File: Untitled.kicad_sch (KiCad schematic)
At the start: 20 parts, among them J1 Battery Connector, J2 Top Screw Terminal, J3 Bottom Screw Terminal, Q1 Q_NMOS_DGS, Q2 Q_NMOS_DGS, Q3 Q_NMOS_DGS, U1 XIAO-ESP32-S3-SMD, U3 LSM6DSO32, U4 MS5611-01BA

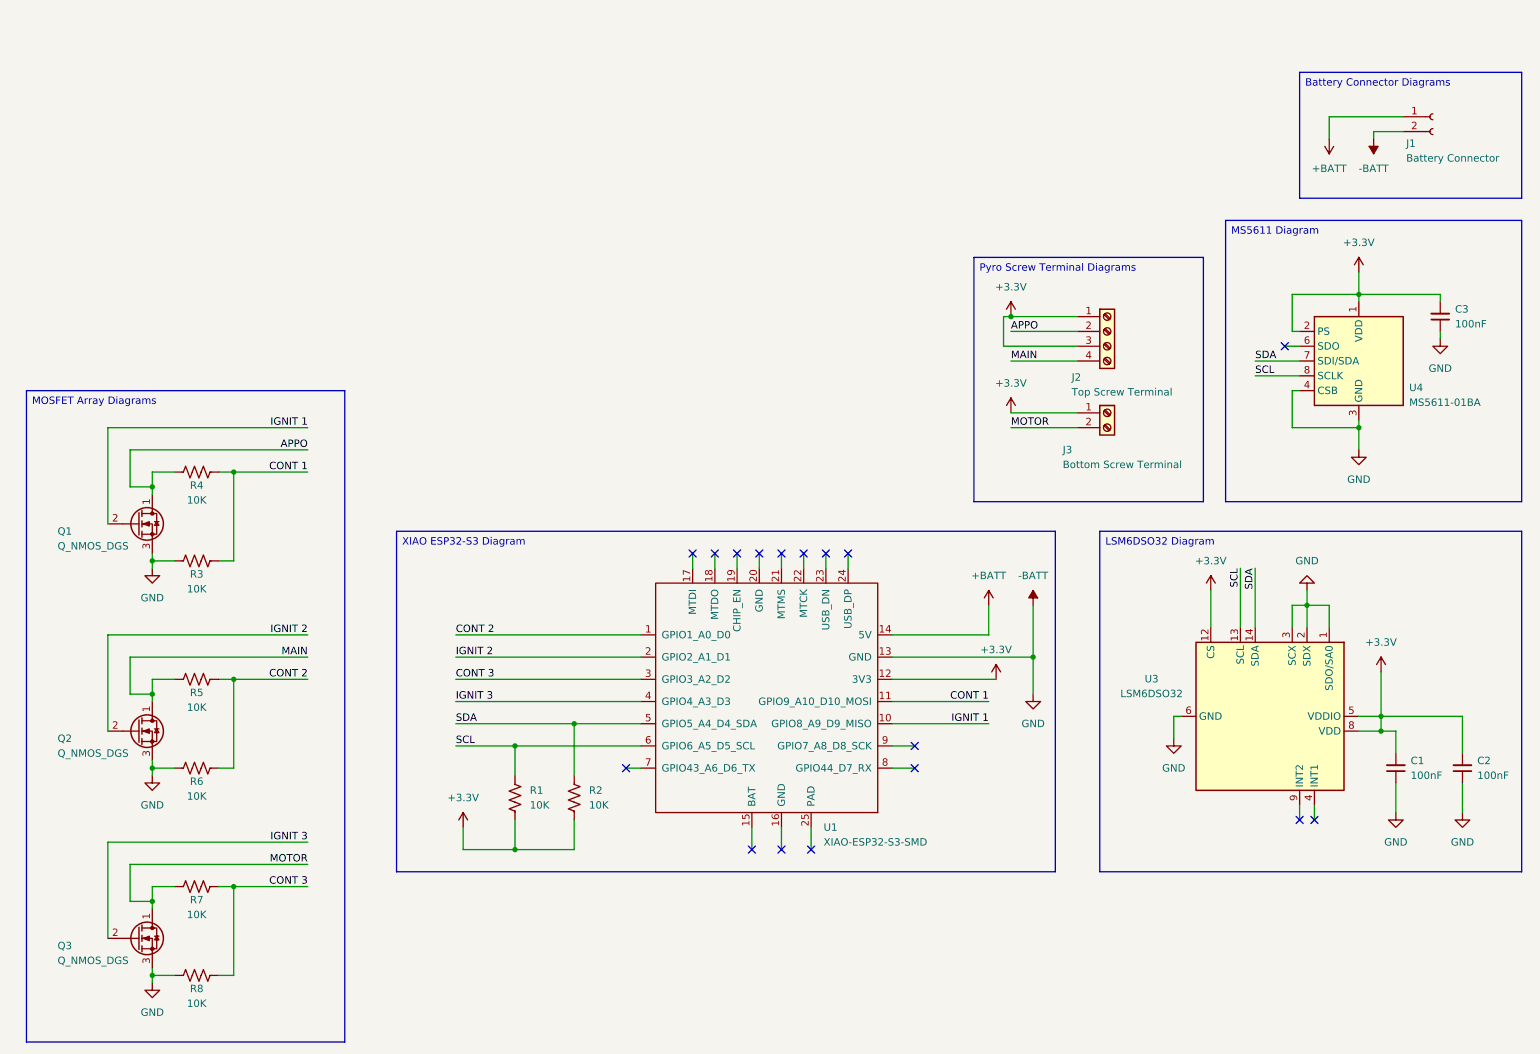
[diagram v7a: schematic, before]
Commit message: Hole Updates and Initial Names
Updated the threaded rod holes to extend to the PCB edge due to them previously leaving such a small gap near the sides of the holes. Drill footprints still there for now, will be removed in final version. Added initial names for every member of the avionics team in alphabetical order. Updated schematic to reflect current state of PCB connections, specifically with the locations of the pyro pins.
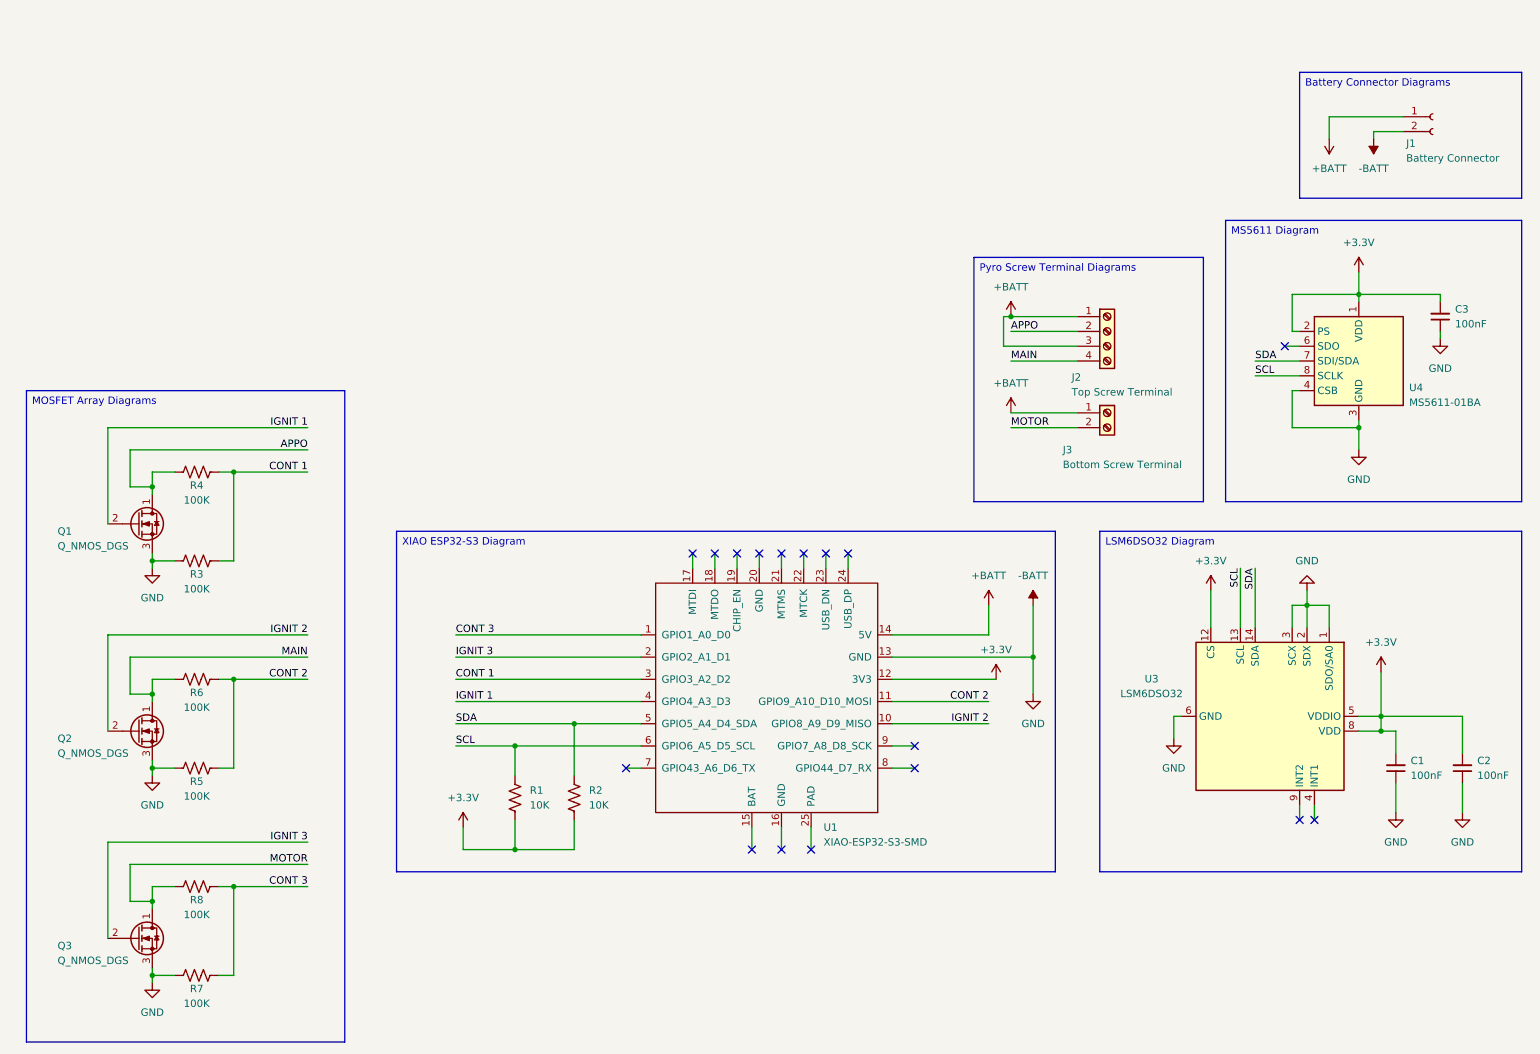
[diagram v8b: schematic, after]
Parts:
- R3, R4: value 10K -> 100K
- R5: renamed from R6; value 10K -> 100K
- R6: renamed from R5; value 10K -> 100K
- R7: renamed from R8; value 10K -> 100K
- R8: renamed from R7; value 10K -> 100K
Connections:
- net +3.3V: no longer J2.1 (Pin_1), J2.3 (Pin_3), J3.1 (Pin_1)
- net +BATT: now also J2.1 (Pin_1), J2.3 (Pin_3), J3.1 (Pin_1)
- net CONT 1: now also U1.3 (GPIO3_A2_D2); no longer U1.11 (GPIO9_A10_D10_MOSI)
- net CONT 2: now also U1.11 (GPIO9_A10_D10_MOSI); no longer U1.1 (GPIO1_A0_D0)
- net CONT 3: now also U1.1 (GPIO1_A0_D0); no longer U1.3 (GPIO3_A2_D2)
- net IGNIT 1: now also U1.4 (GPIO4_A3_D3); no longer U1.10 (GPIO8_A9_D9_MISO)
- net IGNIT 2: now also U1.10 (GPIO8_A9_D9_MISO); no longer U1.2 (GPIO2_A1_D1)
- net IGNIT 3: now also U1.2 (GPIO2_A1_D1); no longer U1.4 (GPIO4_A3_D3)
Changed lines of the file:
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@@
 	)
 	(junction
-		(at 44.45 144.78)
+		(at 191.77 67.31)
 		(diameter 0)
 		(color 0 0 0 0)
 	)
 	(junction
-		(at 58.42 165.1)
+		(at 44.45 144.78)
 		(diameter 0)
 		(color 0 0 0 0)
 	)
 	(junction
-		(at 191.77 67.31)
+		(at 58.42 165.1)
 		(diameter 0)
 		(color 0 0 0 0)
@@
 	(wire
 		(pts
+			(xy 191.77 67.31) (xy 203.2 67.31)
+		)
+		(stroke
+			(width 0)
+			(type default)
+		)
+	)
+	(wire
+		(pts
 			(xy 251.46 135.89) (xy 255.27 135.89)
 		)
@@
 	(wire
 		(pts
-			(xy 191.77 67.31) (xy 203.2 67.31)
-		)
-		(stroke
-			(width 0)
-			(type default)
-		)
-	)
-	(wire
-		(pts
 			(xy 269.24 152.4) (xy 269.24 147.32)
 		)
@@
 		)
 	)
-	(label "IGNIT 1"
+	(label "IGNIT 2"
 		(at 187.96 137.16 180)
 		(effects
@@
 		)
 	)
-	(label "IGNIT 2"
+	(label "IGNIT 3"
 		(at 96.52 125.73 0)
 		(effects
@@
 		)
 	)
-	(label "CONT 1"
+	(label "CONT 2"
 		(at 187.96 133.35 180)
 		(effects
@@
 		)
 	)
-	(label "IGNIT 3"
+	(label "IGNIT 1"
 		(at 96.52 133.35 0)
 		(effects
@@
 		)
 	)
-	(label "CONT 3"
+	(label "CONT 1"
 		(at 96.52 129.54 0)
 		(effects
@@
 		)
 	)
-	(label "CONT 2"
+	(label "CONT 3"
 		(at 96.52 121.92 0)
 		(effects
@@
 	)
 	(symbol
-		(lib_id "power:+3.3V")
-		(at 191.77 83.82 0)
+		(lib_id "power:GND")
+		(at 44.45 110.49 0)
 		(unit 1)
 		(exclude_from_sim no)
@@
 		(dnp no)
 		(fields_autoplaced yes)
-		(property "Reference" "#PWR021"
-			(at 191.77 87.63 0)
+		(property "Reference" "#PWR02"
+			(at 44.45 116.84 0)
 			(effects
 				(font
@@
 			)
 		)
-		(property "Value" "+3.3V"
-			(at 191.77 78.74 0)
+		(property "Value" "GND"
+			(at 44.45 115.57 0)
 			(effects
 				(font
@@
 		)
 		(property "Footprint" ""
-			(at 191.77 83.82 0)
+			(at 44.45 110.49 0)
 			(effects
 				(font
@@
 		)
 		(property "Datasheet" ""
-			(at 191.77 83.82 0)
+			(at 44.45 110.49 0)
 			(effects
 				(font
@@
 			)
 		)
-		(property "Description" "Power symbol creates a global label with name \"+3.3V\""
-			(at 191.77 83.82 0)
+		(property "Description" "Power symbol creates a global label with name \"GND\" , ground"
+			(at 44.45 110.49 0)
 			(effects
 				(font
@@
 			(project "Untitled"
 				(path "/de1c2513-dd99-4dc0-9685-67272008b11d"
-					(reference "#PWR021")
+					(reference "#PWR02")
 					(unit 1)
 				)
@@
 	)
 	(symbol
-		(lib_id "power:GND")
-		(at 44.45 110.49 0)
+		(lib_id "power:+BATT")
+		(at 191.77 83.82 0)
 		(unit 1)
 		(exclude_from_sim no)
@@
 		(dnp no)
 		(fields_autoplaced yes)
-		(property "Reference" "#PWR02"
-			(at 44.45 116.84 0)
+		(property "Reference" "#PWR021"
+			(at 191.77 87.63 0)
 			(effects
 				(font
@@
 			)
 		)
-		(property "Value" "GND"
-			(at 44.45 115.57 0)
+		(property "Value" "+BATT"
+			(at 191.77 78.74 0)
 			(effects
 				(font
@@
 		)
 		(property "Footprint" ""
-			(at 44.45 110.49 0)
+			(at 191.77 83.82 0)
 			(effects
 				(font
@@
 		)
 		(property "Datasheet" ""
-			(at 44.45 110.49 0)
+			(at 191.77 83.82 0)
 			(effects
 				(font
@@
 			)
 		)
-		(property "Description" "Power symbol creates a global label with name \"GND\" , ground"
-			(at 44.45 110.49 0)
+		(property "Description" "Power symbol creates a global label with name \"+BATT\""
+			(at 191.77 83.82 0)
 			(effects
 				(font
@@
 			(project "Untitled"
 				(path "/de1c2513-dd99-4dc0-9685-67272008b11d"
-					(reference "#PWR02")
+					(reference "#PWR021")
 					(unit 1)
 				)
@@
 			)
 		)
-		(property "Value" "10K"
+		(property "Value" "100K"
 			(at 52.07 98.806 90)
 			(effects
@@
 	)
 	(symbol
-		(lib_id "power:+3.3V")
-		(at 191.77 67.31 0)
-		(unit 1)
-		(exclude_from_sim no)
-		(in_bom yes)
-		(on_board yes)
-		(dnp no)
-		(fields_autoplaced yes)
-		(property "Reference" "#PWR020"
-			(at 191.77 71.12 0)
-			(effects
-				(font
-					(size 1.27 1.27)
-				)
-				(hide yes)
-			)
-		)
-		(property "Value" "+3.3V"
-			(at 191.77 62.23 0)
-			(effects
-				(font
-					(size 1.27 1.27)
-				)
-			)
-		)
-		(property "Footprint" ""
-			(at 191.77 67.31 0)
-			(effects
-				(font
-					(size 1.27 1.27)
-				)
-				(hide yes)
-			)
-		)
-		(property "Datasheet" ""
-			(at 191.77 67.31 0)
-			(effects
-				(font
-					(size 1.27 1.27)
-				)
-				(hide yes)
-			)
-		)
-		(property "Description" "Power symbol creates a global label with name \"+3.3V\""
-			(at 191.77 67.31 0)
-			(effects
-				(font
-					(size 1.27 1.27)
-				)
-				(hide yes)
-			)
-		)
-		(pin "1"
-		)
-		(instances
-			(project "Untitled"
-				(path "/de1c2513-dd99-4dc0-9685-67272008b11d"
-					(reference "#PWR020")
-					(unit 1)
-				)
-			)
-		)
-	)
-	(symbol
 		(lib_id "Transistor_FET:Q_NMOS_DGS")
 		(at 41.91 102.87 0)
@@
 		(on_board yes)
 		(dnp no)
-		(property "Reference" "R6"
+		(property "Reference" "R5"
 			(at 52.07 147.066 90)
 			(effects
@@
 			)
 		)
-		(property "Value" "10K"
+		(property "Value" "100K"
 			(at 52.07 149.606 90)
 			(effects
@@
 			(project "Untitled"
 				(path "/de1c2513-dd99-4dc0-9685-67272008b11d"
-					(reference "R6")
+					(reference "R5")
 					(unit 1)
 				)
@@
 			)
 		)
-		(property "Value" "10K"
+		(property "Value" "100K"
 			(at 52.07 114.046 90)
 			(effects
@@
 		(on_board yes)
 		(dnp no)
-		(property "Reference" "R7"
+		(property "Reference" "R8"
 			(at 52.07 167.386 90)
 			(effects
@@
 			)
 		)
-		(property "Value" "10K"
+		(property "Value" "100K"
 			(at 52.07 169.926 90)
 			(effects
@@
 			(project "Untitled"
 				(path "/de1c2513-dd99-4dc0-9685-67272008b11d"
-					(reference "R7")
+					(reference "R8")
 					(unit 1)
 				)
@@
 		(on_board yes)
 		(dnp no)
-		(property "Reference" "R5"
+		(property "Reference" "R6"
 			(at 52.07 131.826 90)
 			(effects
@@
 			)
 		)
-		(property "Value" "10K"
+		(property "Value" "100K"
 			(at 52.07 134.366 90)
 			(effects
@@
 			(project "Untitled"
 				(path "/de1c2513-dd99-4dc0-9685-67272008b11d"
-					(reference "R5")
+					(reference "R6")
 					(unit 1)
 				)
@@
 		(on_board yes)
 		(dnp no)
-		(property "Reference" "R8"
+		(property "Reference" "R7"
 			(at 52.07 182.626 90)
 			(effects
@@
 			)
 		)
-		(property "Value" "10K"
+		(property "Value" "100K"
 			(at 52.07 185.166 90)
 			(effects
@@
 			(project "Untitled"
 				(path "/de1c2513-dd99-4dc0-9685-67272008b11d"
-					(reference "R8")
+					(reference "R7")
 					(unit 1)
 				)
@@
 					(unit 1)
 				)
+			)
+		)
+	)
+	(symbol
+		(lib_id "power:+BATT")
+		(at 191.77 67.31 0)
+		(unit 1)
+		(exclude_from_sim no)
+		(in_bom yes)
+		(on_board yes)
+		(dnp no)
+		(fields_autoplaced yes)
+		(property "Reference" "#PWR020"
+			(at 191.77 71.12 0)
+			(effects
+				(font
+					(size 1.27 1.27)
+				)
+				(hide yes)
+			)
+		)
+		(property "Value" "+BATT"
+			(at 191.77 62.23 0)
+			(effects
+				(font
+					(size 1.27 1.27)
+				)
+			)
+		)
+		(property "Footprint" ""
+			(at 191.77 67.31 0)
+			(effects
+				(font
+					(size 1.27 1.27)
+				)
+				(hide yes)
+			)
+		)
+		(property "Datasheet" ""
+			(at 191.77 67.31 0)
+			(effects
+				(font
+					(size 1.27 1.27)
+				)
+				(hide yes)
+			)
+		)
+		(property "Description" "Power symbol creates a global label with name \"+BATT\""
+			(at 191.77 67.31 0)
+			(effects
+				(font
+					(size 1.27 1.27)
+				)
+				(hide yes)
+			)
+		)
+		(pin "1"
+		)
+		(instances
+			(project "Untitled"
+				(path "/de1c2513-dd99-4dc0-9685-67272008b11d"
+					(reference "#PWR020")
+					(unit 1)
+				)
